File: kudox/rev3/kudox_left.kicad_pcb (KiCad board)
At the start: 2 copper layers, 145.9 x 129.8 mm, 90 parts, among them K0 KEYSW, K1 KEYSW, K10 KEYSW, K11 KEYSW, K12 KEYSW, K13 KEYSW, K14 KEYSW, K15 KEYSW, K16 KEYSW, K2 KEYSW, K20 KEYSW, K21 KEYSW, K22 KEYSW, K23 KEYSW, K24 KEYSW, K25 KEYSW, K3 KEYSW, K30 KEYSW, K31 KEYSW, K32 KEYSW, K33 KEYSW, K34 KEYSW, K35 KEYSW, K4 KEYSW, K40 KEYSW, K41 KEYSW, K42 KEYSW, K43 KEYSW, K44 KEYSW, K45 KEYSW, K46 KEYSW, K5 KEYSW, K6 KEYSW, U1 ProMicro

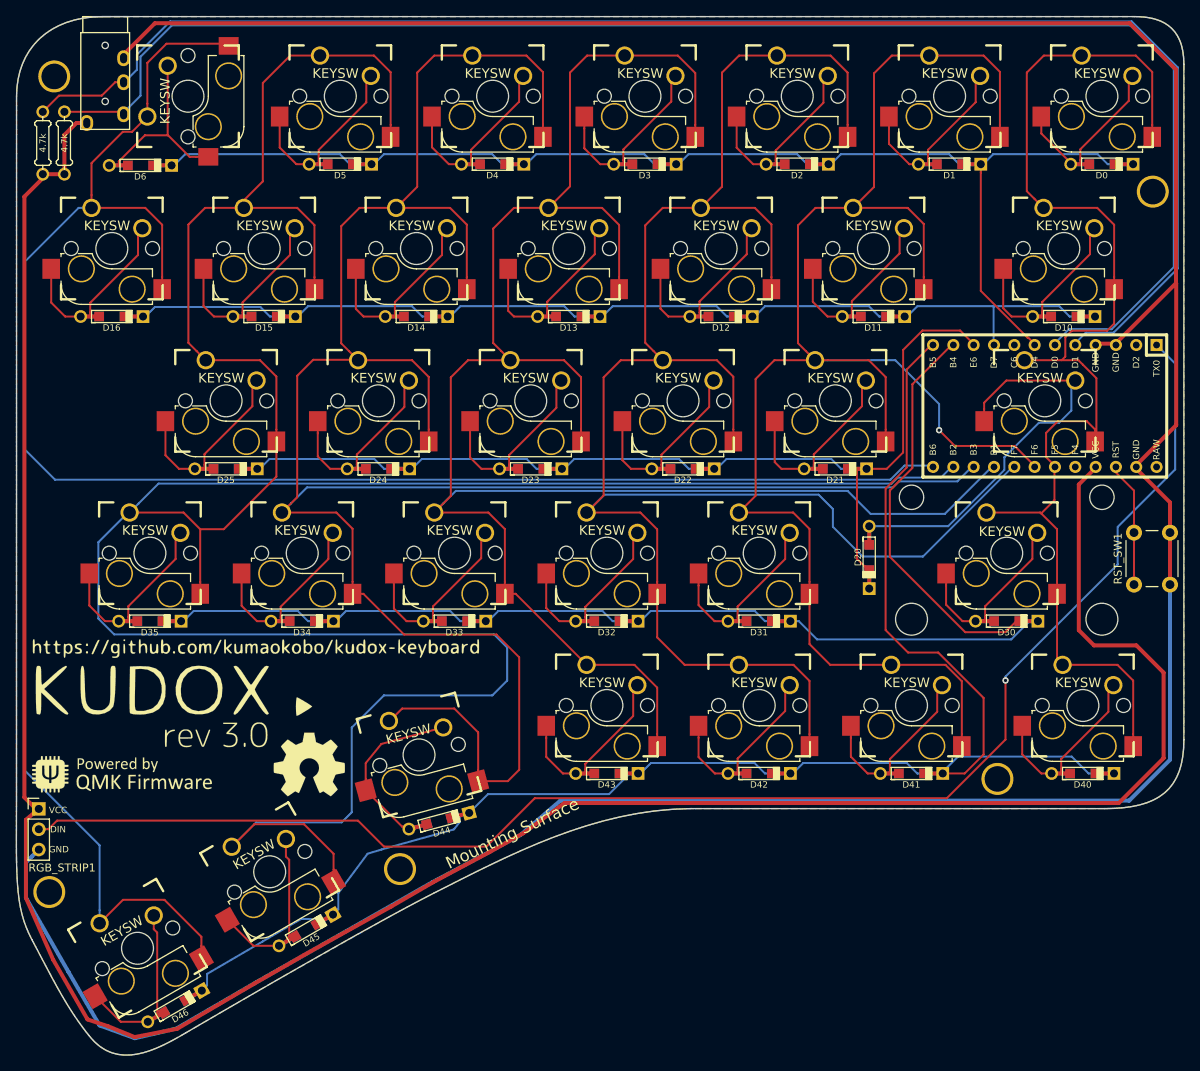
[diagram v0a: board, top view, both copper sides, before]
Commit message: Modify kudox/rev3 to add RGB pad
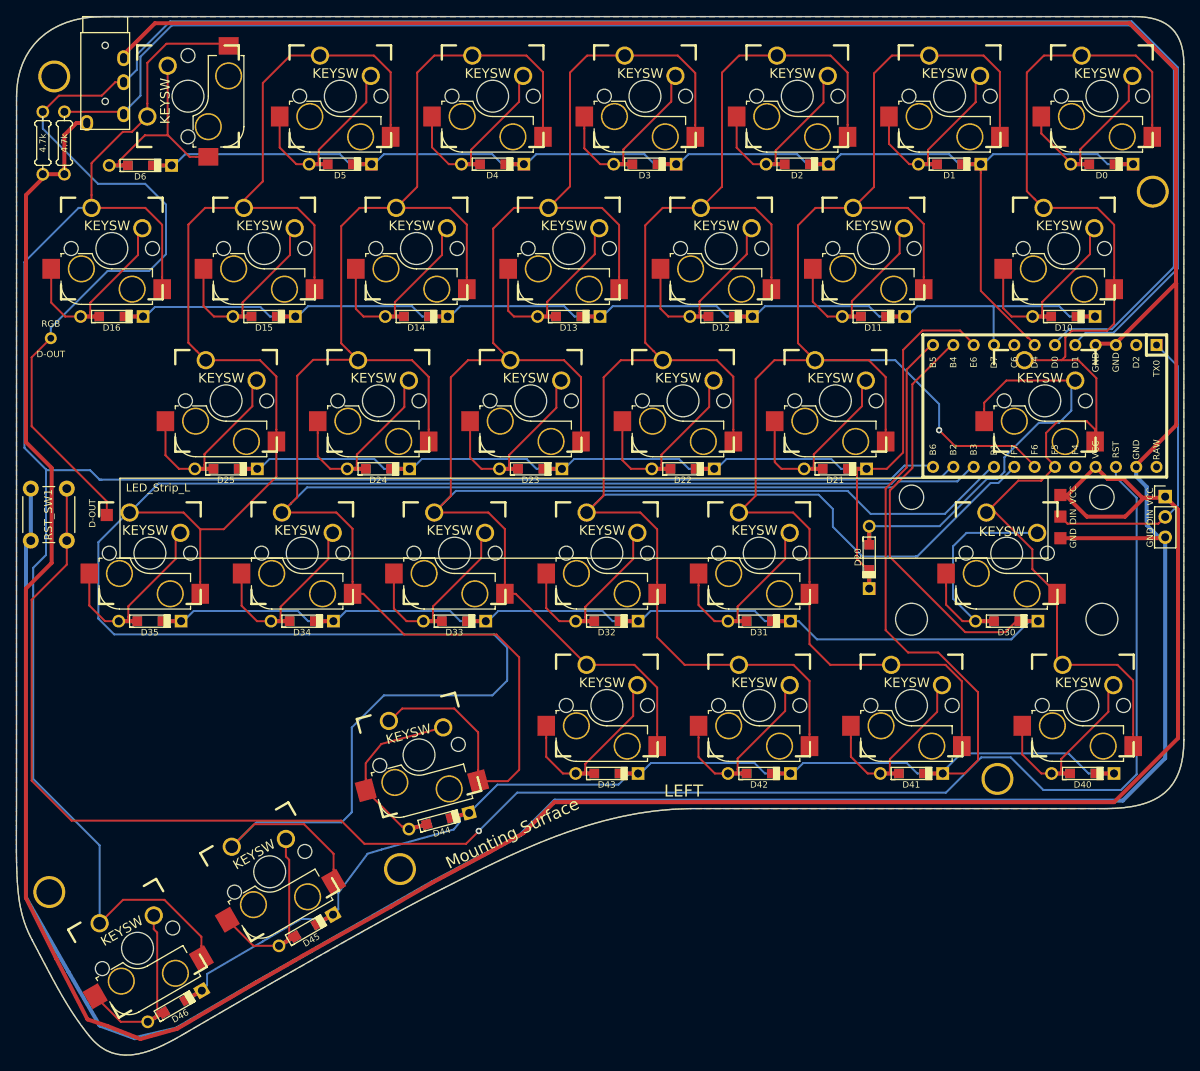
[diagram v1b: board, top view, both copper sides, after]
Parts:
- removed the G*** at (83.2, 124.7)
- removed the G*** at (95.1, 119.7)
- removed the G*** at (83.9, 119.7)
- removed REF*** (x2): OSHW-Logo2_14.6x12mm_SilkScreen, kudox_footprints:OSHW-Symbol_8.9x8mm_SilkScreen
- added G***: LOGO, kudox_footprints:version, B.Cu at (82.7, 120.6)
- added G***: LOGO, kudox_footprints:version, F.Cu at (112.1, 113.6)
- added G***: LOGO, kudox_footprints:qmk-badge-mask, F.Cu at (90.0, 125.0)
- added G***: LOGO, kudox_footprints:copyright, B.Cu at (97.9, 120.5)
- added G***: LOGO, kudox_footprints:copyright, F.Cu at (93.5, 120.5)
- added J1: D-OUT, kudox_footprints:Pin_Header_Straight_1x01_Pitch2.54mm, F.Cu at (74.3, 70.2)
- added J2: D-OUT, kudox_footprints:rgb_pad, F.Cu at (81.3, 92.3)
- added J3: VCC, kudox_footprints:pad_1x1, F.Cu at (200.5, 89.8)
- added J4: DIN, kudox_footprints:pad_1x1, F.Cu at (200.5, 92.5)
- added J5: GND, kudox_footprints:pad_1x1, F.Cu at (200.5, 95.2)
- added REF**: LED_Strip_L, kudox_footprints:LED_Strip_L, F.Cu at (140.9, 92.7)
- G*** (x2): footprint kudox_footprints:kudox-logo -> kudox_footprints:kudox-logo-mask
- G*** (x2): footprint kudox_footprints:kudox_github_silk -> kudox_footprints:kudox_github
- G***: footprint kudox_footprints:qmk-badge -> kudox_footprints:qmk-badge-mask
- moved RGB_STRIP1 146.1 mm to (213.6, 90.0)
- moved RST_SW1 133.9 mm to (76.3, 89.0), turned to 270 degrees
- moved G*** 6.06 mm to (91.3, 125.0)
- moved G*** 1.12 mm to (90.2, 115.2)
- moved G*** 1.02 mm to (89.1, 115.2)
- moved G*** 0.71 mm to (100.5, 109.5) (x2)
- moved G*** 0.47 mm to (78.5, 78.5) (x2)
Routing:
- net RST: track 15.8 -> 227.0 mm, vias 0 -> 1
- net rgb_data: track 187.4 -> 37.6 mm, vias 1 -> 0
- net SDA: track 191.9 -> 266.1 mm
- net GND: track 408.9 -> 466.3 mm
- net VCC: track 311.1 -> 330.9 mm
- net Net-(D30-Pad2): track 22.2 -> 30.2 mm
- net col0: track 157.7 -> 159.9 mm
- net col6: track 282.8 -> 280.8 mm

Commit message: Compatible with ProMicro Type-C
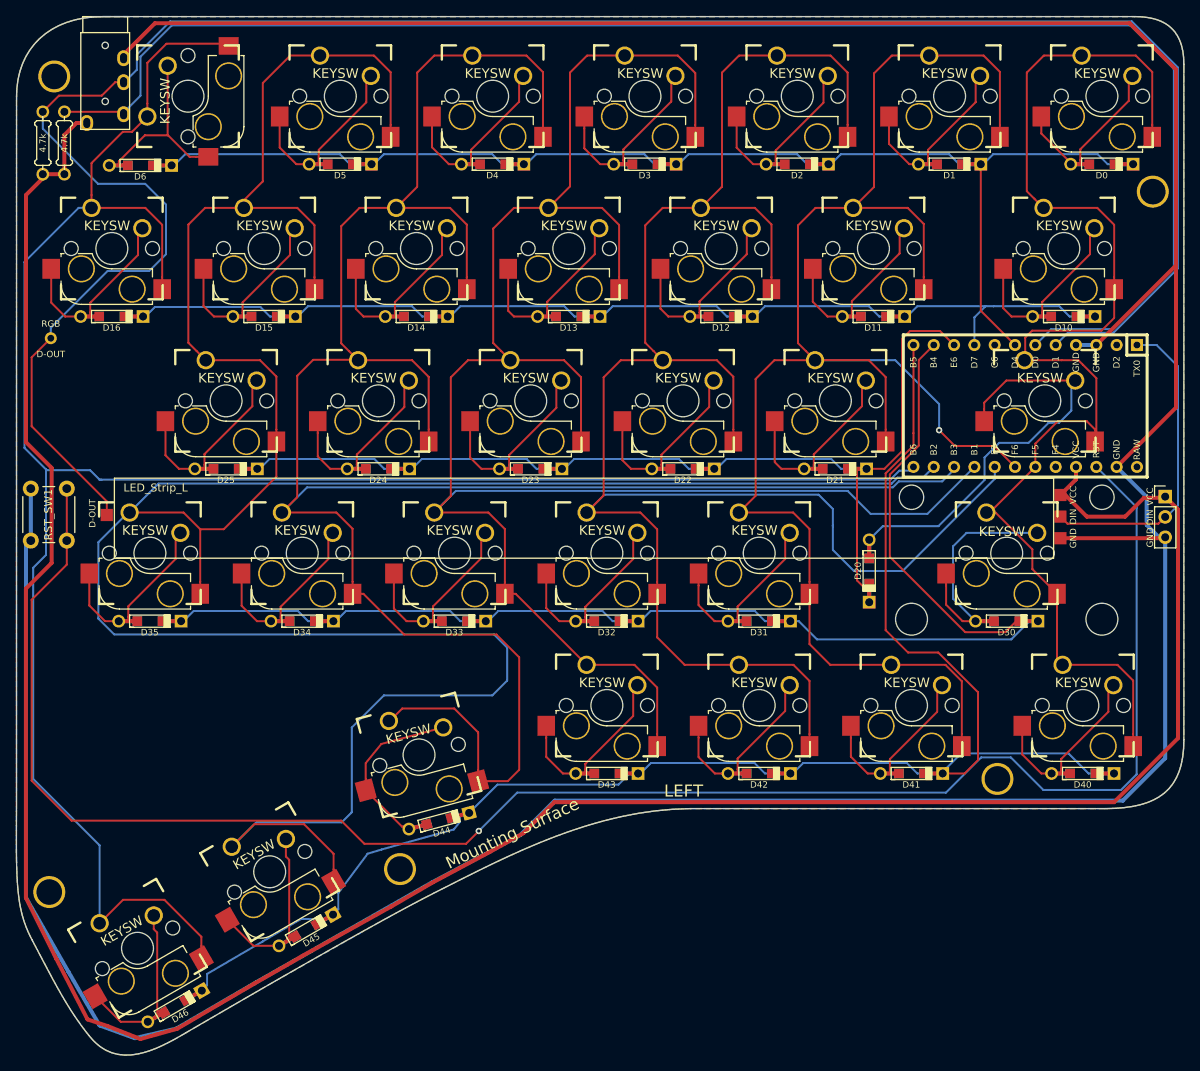
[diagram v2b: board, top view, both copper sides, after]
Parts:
- U1: footprint kudox_footprints:ArduinoProMicro -> kudox_footprints:ArduinoProMicroTypeC
- moved U1 2.45 mm to (196.1, 78.7)
- moved D20 1.70 mm to (176.6, 99.3)
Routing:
- net VCC: track 330.9 -> 320.7 mm
- net GND: track 466.3 -> 471.6 mm
- net SDA: track 266.1 -> 268.5 mm
- net col3: track 254.1 -> 251.6 mm
- net SCL: track 192.3 -> 194.7 mm
- net col6: track 280.8 -> 278.4 mm
- net col5: track 383.7 -> 381.3 mm
- net col1: track 218.5 -> 216.2 mm
- net col4: track 300.5 -> 298.3 mm
- net rgb_data: track 37.6 -> 39.8 mm
- net col2: track 247.0 -> 248.8 mm
- net col0: track 159.9 -> 161.5 mm
- net Net-(D20-Pad2): track 51.1 -> 52.4 mm
- net row4: track 192.6 -> 191.4 mm
- net row3: track 160.4 -> 159.2 mm
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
